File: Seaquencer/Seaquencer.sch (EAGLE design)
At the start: 39 parts, among them IC2 74HC595N, SW2 EC12E_SW

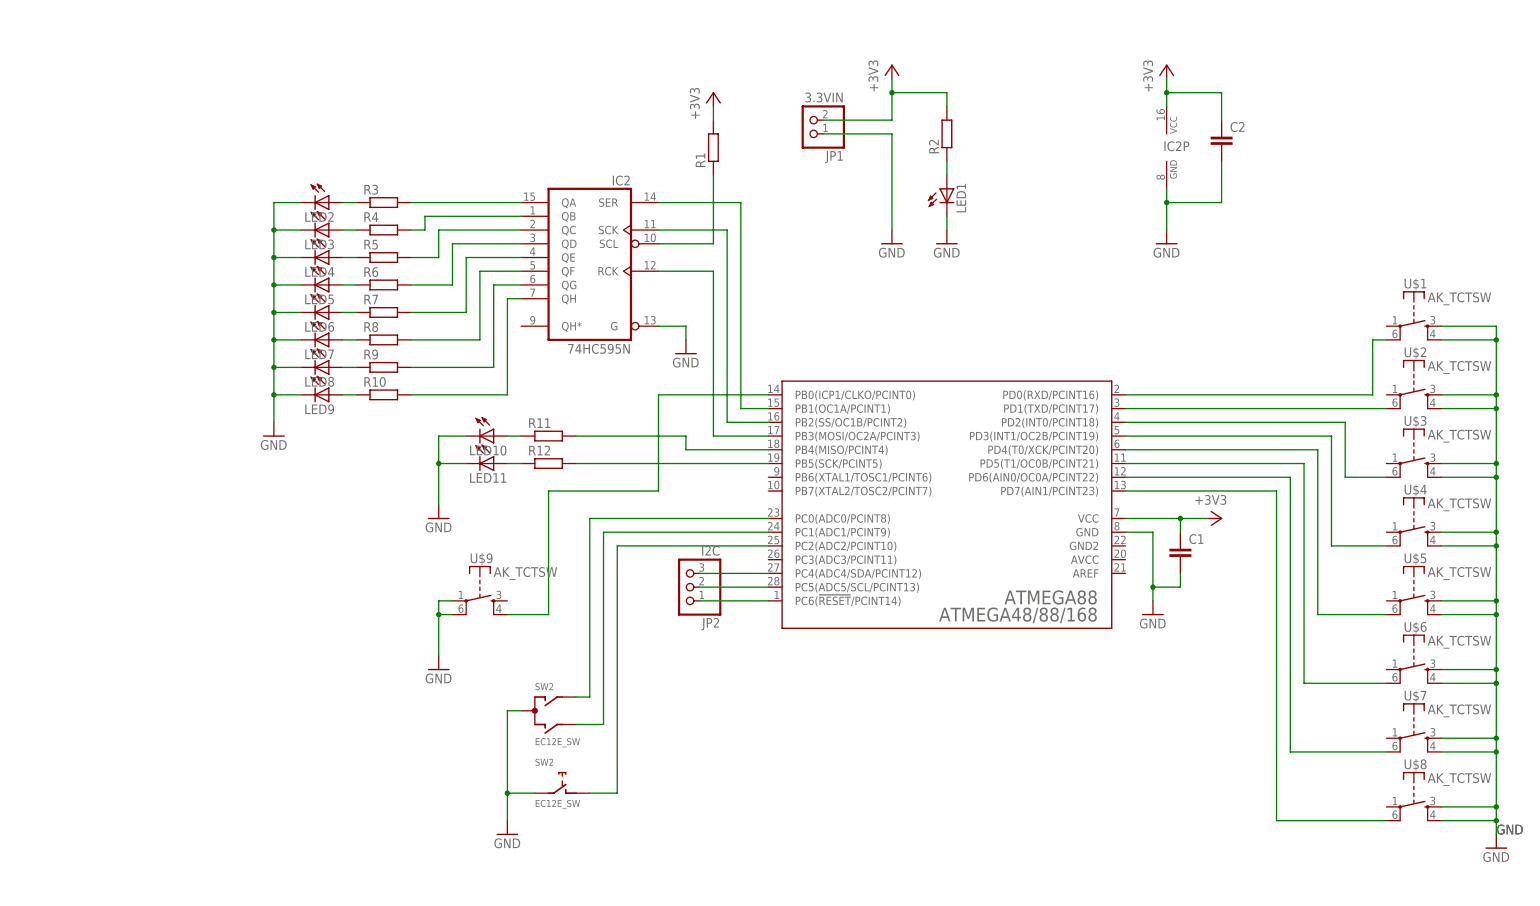
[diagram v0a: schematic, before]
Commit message: Sequencer: POT追加前（完成形）
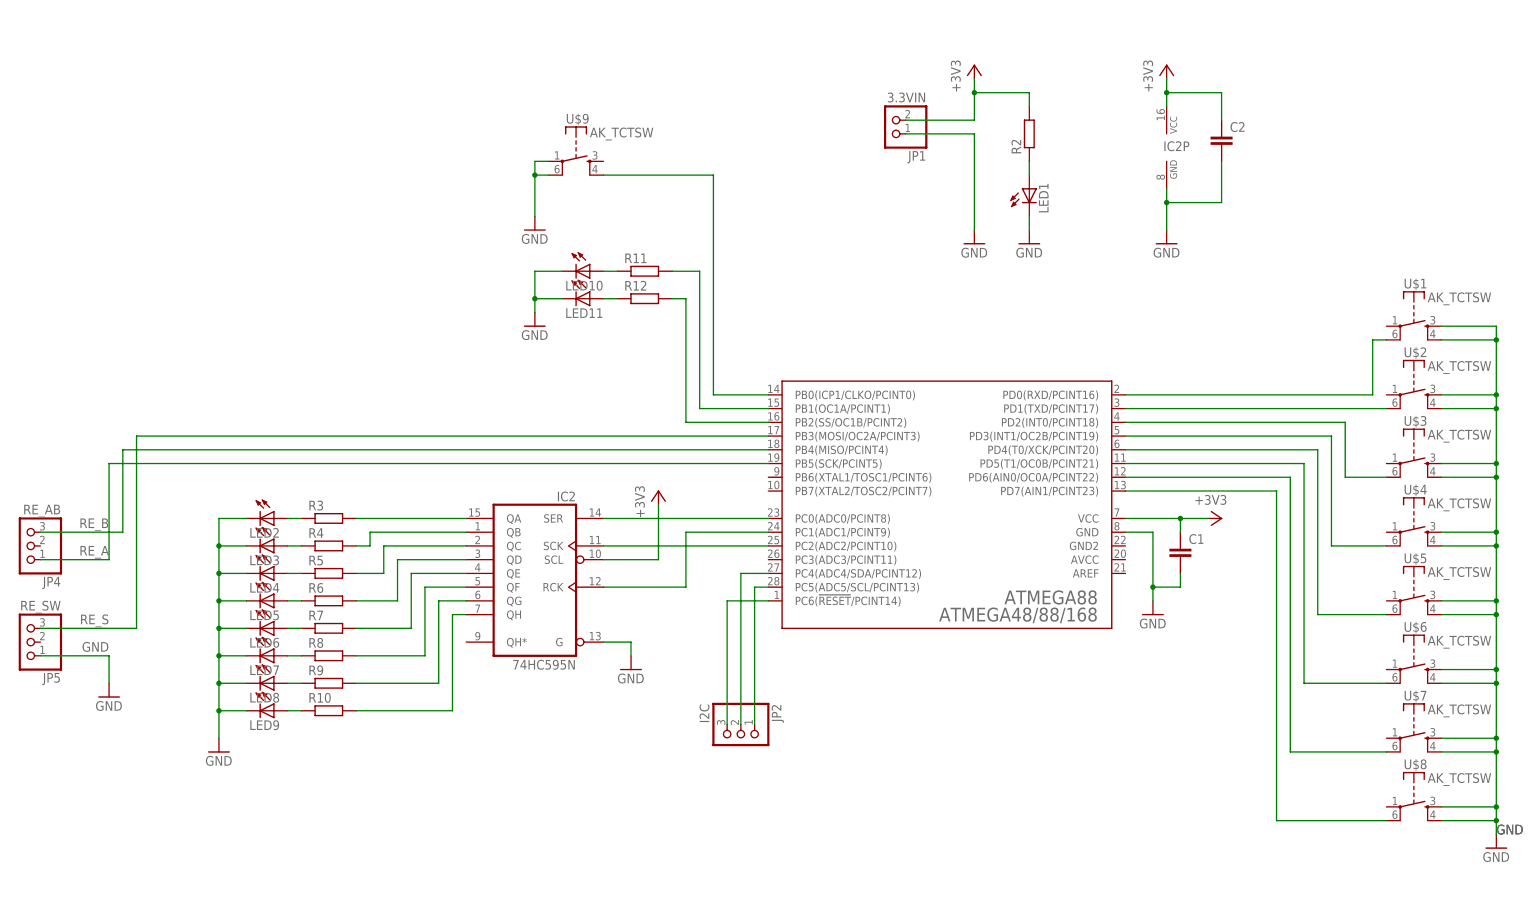
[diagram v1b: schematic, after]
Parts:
- removed R1: (no value), rcl:R-EU_0207/7
- removed SW2: EC12E_SW, switch-alps:EC12E_SW
- added JP4: RE_AB, pinhead:PINHD-1X3
- added JP5: RE_SW, pinhead:PINHD-1X3
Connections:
- removed net N$10: ATMEGA88.PC4(ADC4/SDA/PCINT12), JP2.3
- removed net N$14: IC2A.SCL, R1.1
- removed net N$37: ATMEGA88.PC0(ADC0/PCINT8), SW2G$1.A
- removed net N$38: ATMEGA88.PC1(ADC1/PCINT9), SW2G$1.B
- removed net N$8: ATMEGA88.PC2(ADC2/PCINT10), SW2G$2.1
- new net N$42: ATMEGA88.PC6(!RESET!/PCINT14), JP2.3
- new net RE_A: ATMEGA88.PB4(MISO/PCINT4), JP4.3
- new net RE_B: ATMEGA88.PB5(SCK/PCINT5), JP4.1
- new net RE_S: ATMEGA88.PB3(MOSI/OC2A/PCINT3), JP5.3
- net +3V3: now also IC2A.SCL; no longer R1.2
- net GND: now also JP5.1; no longer SW2G$1.C, SW2G$2.2
- net N$11: now also ATMEGA88.PC0(ADC0/PCINT8); no longer ATMEGA88.PB1(OC1A/PCINT1)
- net N$12: now also ATMEGA88.PC1(ADC1/PCINT9); no longer ATMEGA88.PB3(MOSI/OC2A/PCINT3)
- net N$32: now also ATMEGA88.PC2(ADC2/PCINT10); no longer ATMEGA88.PB2(SS/OC1B/PCINT2)
- net N$35: now also ATMEGA88.PB2(SS/OC1B/PCINT2); no longer ATMEGA88.PB5(SCK/PCINT5)
- net N$36: now also ATMEGA88.PB1(OC1A/PCINT1); no longer ATMEGA88.PB4(MISO/PCINT4)
- net N$39: now also ATMEGA88.PC4(ADC4/SDA/PCINT12), JP2.2; no longer ATMEGA88.PC6(!RESET!/PCINT14), JP2.1
- net N$9: now also JP2.1; no longer JP2.2
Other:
- moved on the sheet: IC2, JP1, JP2, LED1, LED10, LED11, LED2, LED3, LED4, LED5, LED6, LED7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

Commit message: Sequencer: POTを追加
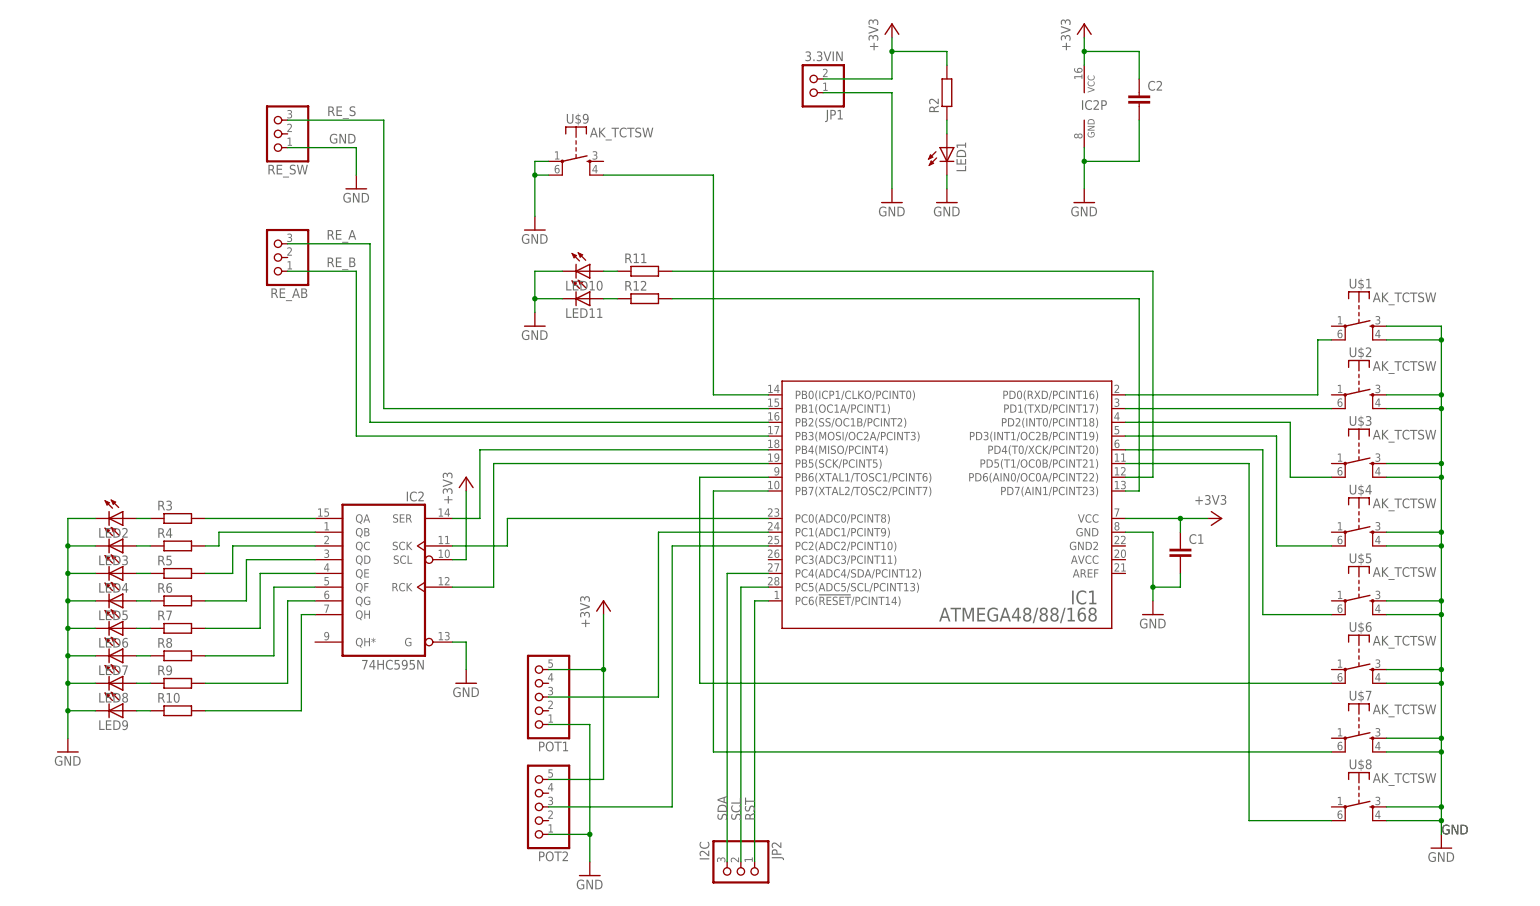
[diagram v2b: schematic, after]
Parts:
- removed JP4: RE_AB, pinhead:PINHD-1X3
- removed JP5: RE_SW, pinhead:PINHD-1X3
- added POT1, POT2: (no value), pinhead:PINHD-1X5
- added RE_AB, RE_SW: (no value), pinhead:PINHD-1X3
- renumbered ATMEGA88 to IC1
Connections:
- removed net N$32: IC1.PC2(ADC2/PCINT10), IC2A.SCK
- removed net N$39: IC1.PC4(ADC4/SDA/PCINT12), JP2.2
- removed net N$42: IC1.PC6(!RESET!/PCINT14), JP2.3
- new net N$10: IC1.PC1(ADC1/PCINT9), POT1.3
- new net N$8: IC1.PB4(MISO/PCINT4), IC2A.SER
- new net RST: IC1.PC6(!RESET!/PCINT14), JP2.1
- new net SCL: IC1.PC5(ADC5/SCL/PCINT13), JP2.2
- new net SDA: IC1.PC4(ADC4/SDA/PCINT12), JP2.3
- net +3V3: now also POT1.5, POT2.5
- net GND: now also POT1.1, POT2.1, RE_SW.1; no longer JP5.1
- net N$11: now also IC1.PC2(ADC2/PCINT10), POT2.3; no longer IC1.PC0(ADC0/PCINT8), IC2A.SER
- net N$12: now also IC1.PB5(SCK/PCINT5); no longer IC1.PC1(ADC1/PCINT9)
- net N$3: now also IC1.PD5(T1/OC0B/PCINT21); no longer IC1.PD7(AIN1/PCINT23)
- net N$35: now also IC1.PD7(AIN1/PCINT23); no longer IC1.PB2(SS/OC1B/PCINT2)
- net N$36: now also IC1.PD6(AIN0/OC0A/PCINT22); no longer IC1.PB1(OC1A/PCINT1)
- net N$4: now also IC1.PB7(XTAL2/TOSC2/PCINT7); no longer IC1.PD6(AIN0/OC0A/PCINT22)
- net N$5: now also IC1.PB6(XTAL1/TOSC1/PCINT6); no longer IC1.PD5(T1/OC0B/PCINT21)
- net N$9: now also IC1.PC0(ADC0/PCINT8), IC2A.SCK; no longer IC1.PC5(ADC5/SCL/PCINT13), JP2.1
- net RE_A: now also IC1.PB2(SS/OC1B/PCINT2), RE_AB.3; no longer IC1.PB4(MISO/PCINT4), JP4.3
- net RE_B: now also IC1.PB3(MOSI/OC2A/PCINT3), RE_AB.1; no longer IC1.PB5(SCK/PCINT5), JP4.1
- net RE_S: now also IC1.PB1(OC1A/PCINT1), RE_SW.3; no longer IC1.PB3(MOSI/OC2A/PCINT3), JP5.3
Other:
- moved on the sheet: C2, IC2, IC2P, JP1, JP2, LED1, LED2, LED3, LED4, LED5, LED6, LED7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
